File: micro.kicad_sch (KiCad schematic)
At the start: 1 part

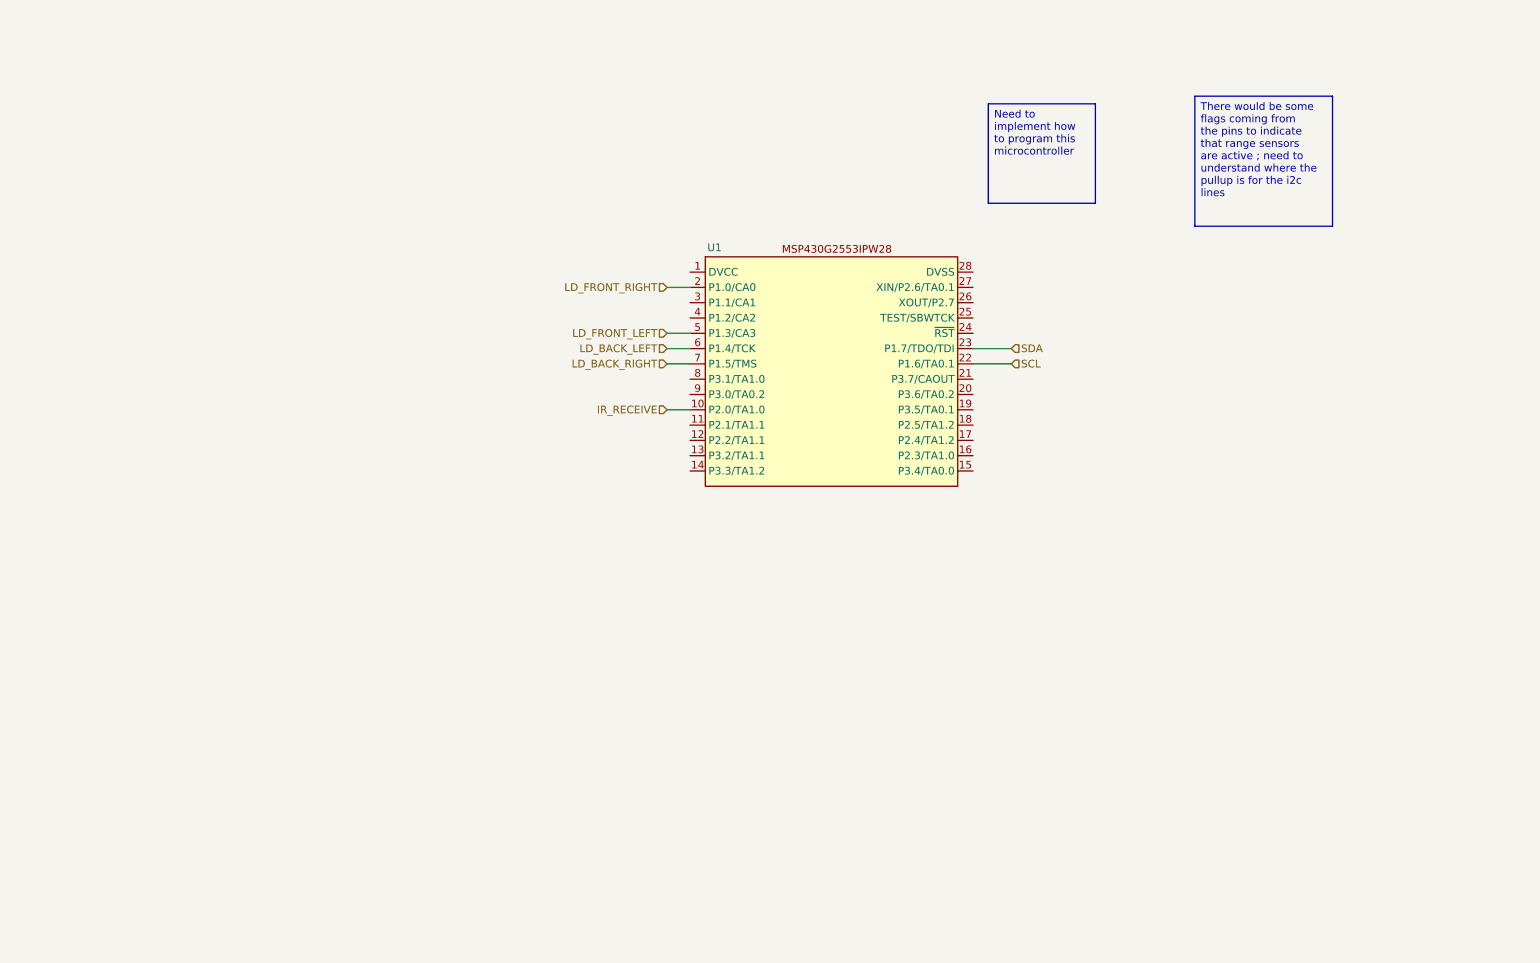
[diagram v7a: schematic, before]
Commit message: added motor functionality to the MCU
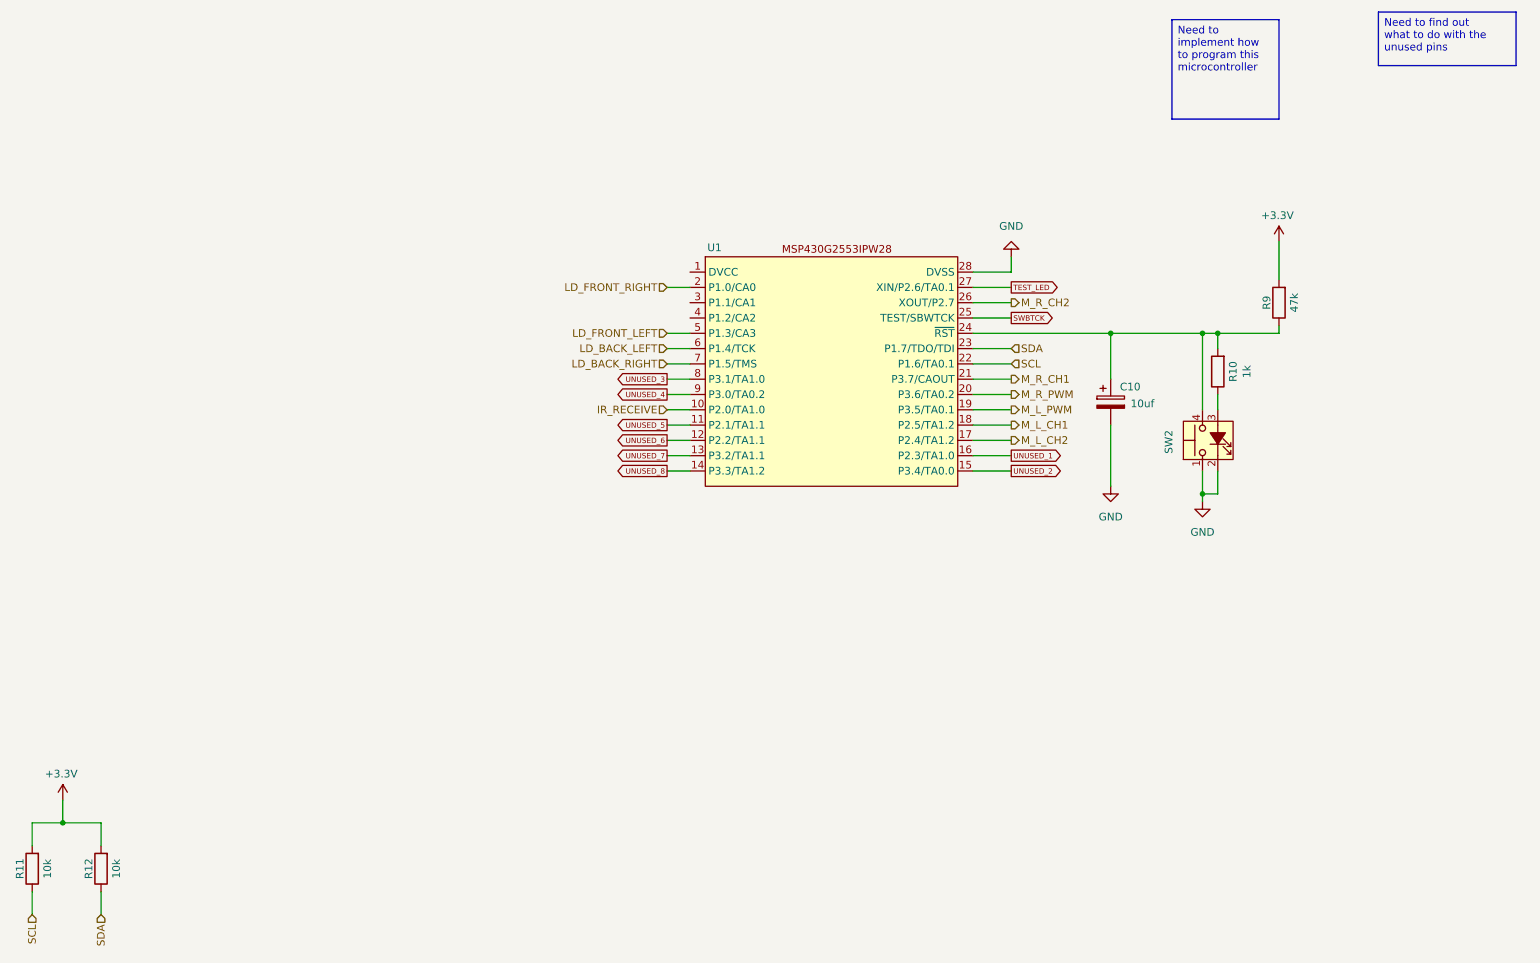
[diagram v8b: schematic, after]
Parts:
- added C10: 10uf, symbol Device:C_Polarized
- added R10: 1k, Resistor_SMD:R_1210_3225Metric, symbol Device:R
- added R11, R12: 10k, Resistor_SMD:R_1210_3225Metric, symbol Device:R
- added R9: 47k, Resistor_SMD:R_1210_3225Metric, symbol Device:R
- added SW2: SW_MEC_5G_LED, symbol Switch:SW_MEC_5G_LED
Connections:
- net SCL: now also R11.1
- net SDA: now also R12.1
- net UNUSED_5: now reaches U1.11 (P2.1/TA1.1)
- net UNUSED_6: now reaches U1.12 (P2.2/TA1.1)
- net UNUSED_7: now reaches U1.13 (P3.2/TA1.1)
- net UNUSED_8: now reaches U1.14 (P3.3/TA1.2)
- net UNUSED_2: now reaches U1.15 (P3.4/TA0.0)
- net UNUSED_1: now reaches U1.16 (P2.3/TA1.0)
- net M_L_CH2: now reaches U1.17 (P2.4/TA1.2)
- net M_L_CH1: now reaches U1.18 (P2.5/TA1.2)
- net M_L_PWM: now reaches U1.19 (P3.5/TA0.1)
- net M_R_PWM: now reaches U1.20 (P3.6/TA0.2)
- net M_R_CH1: now reaches U1.21 (P3.7/CAOUT)
- net at U1.24 (~{RST}): now also C10.1, R10.2, R9.1, SW2.4 (A)
- net SWBTCK: now reaches U1.25 (TEST/SBWTCK)
- net M_R_CH2: now reaches U1.26 (XOUT/P2.7)
- net TEST_LED: now reaches U1.27 (XIN/P2.6/TA0.1)
- net GND: now reaches U1.28 (DVSS)
- net GND: now also C10.2, SW2.1, SW2.2
- net UNUSED_3: now reaches U1.8 (P3.1/TA1.0)
- net UNUSED_4: now reaches U1.9 (P3.0/TA0.2)
- new net: R10.1, SW2.3 (K)
- new net +3.3V: R11.2, R12.2, R9.2
